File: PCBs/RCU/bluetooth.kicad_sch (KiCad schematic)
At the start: 33 parts

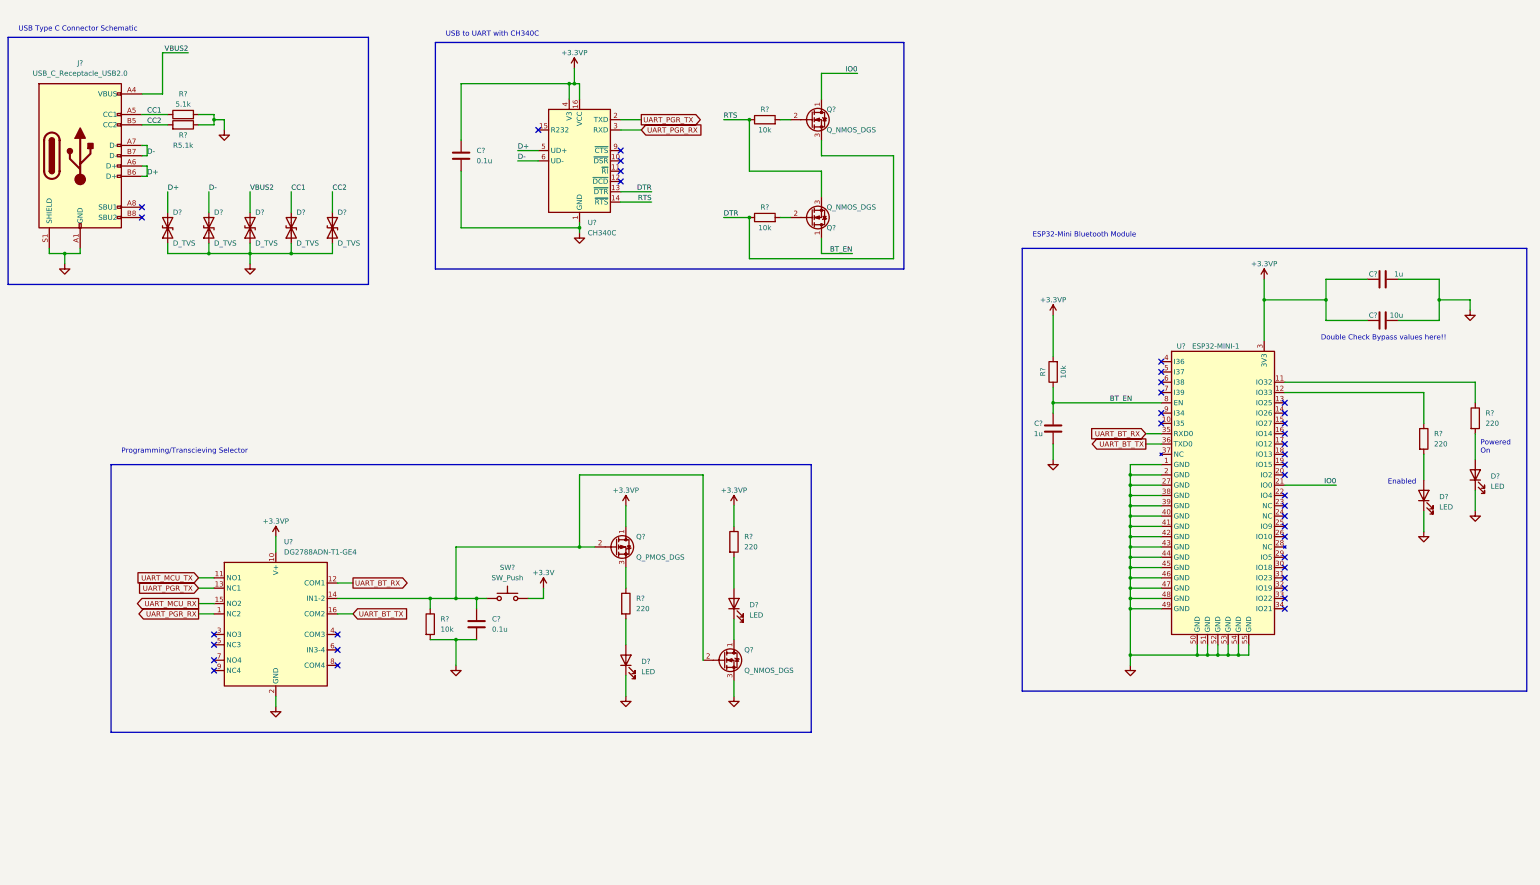
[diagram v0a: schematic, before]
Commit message: Numbered and ordered all of the modules
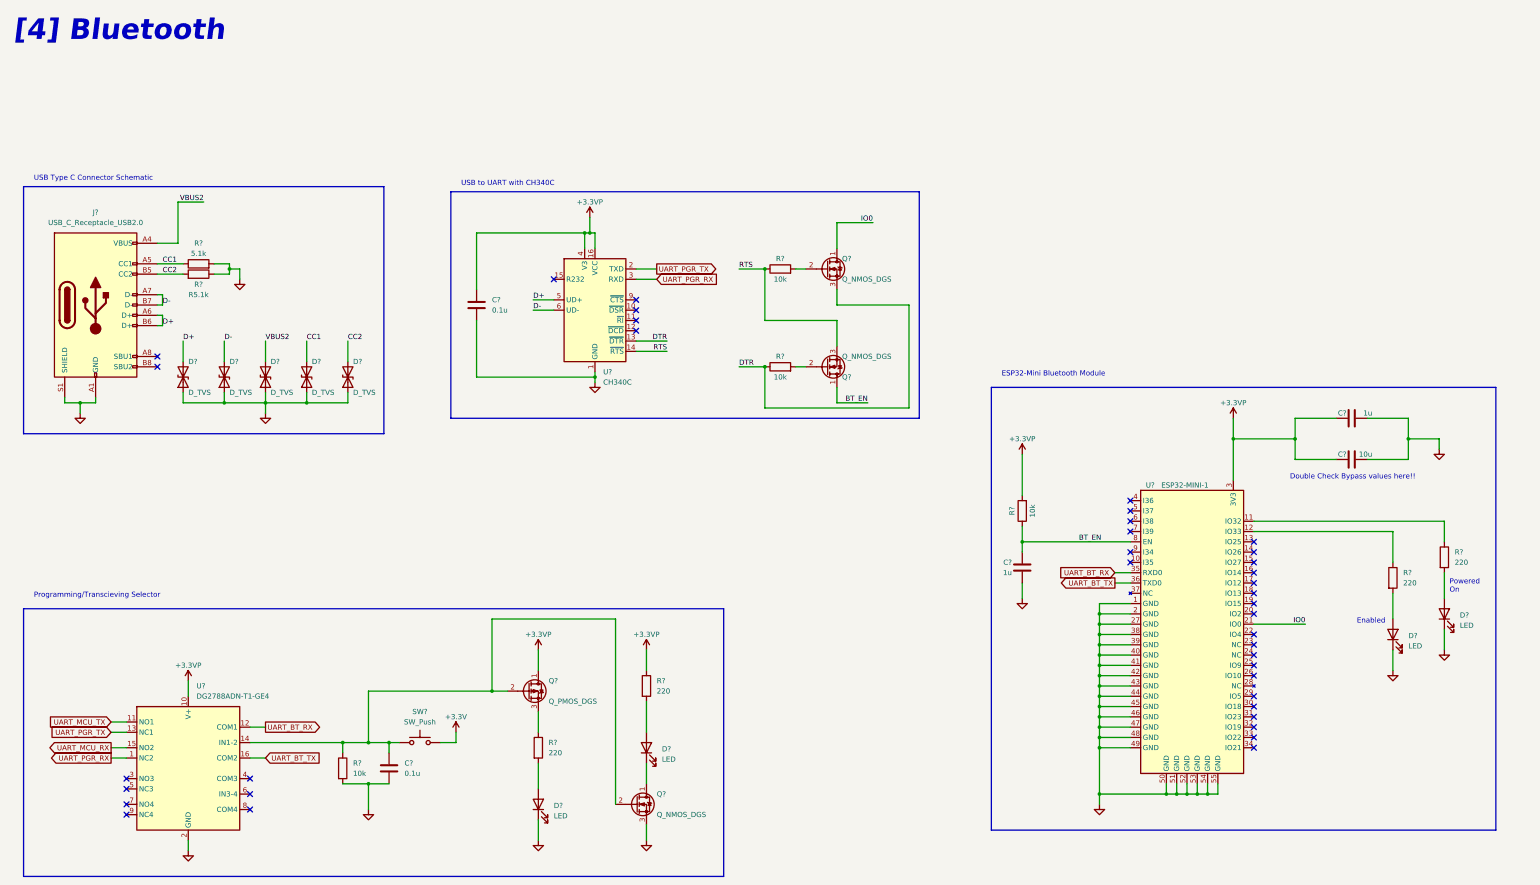
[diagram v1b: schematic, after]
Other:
- note added: "[4] Bluetooth"
- moved on the sheet: C?, D?, J?, Q?, R5.1k, R?, SW?, U?

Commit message: Annotated all components in Bluetooth
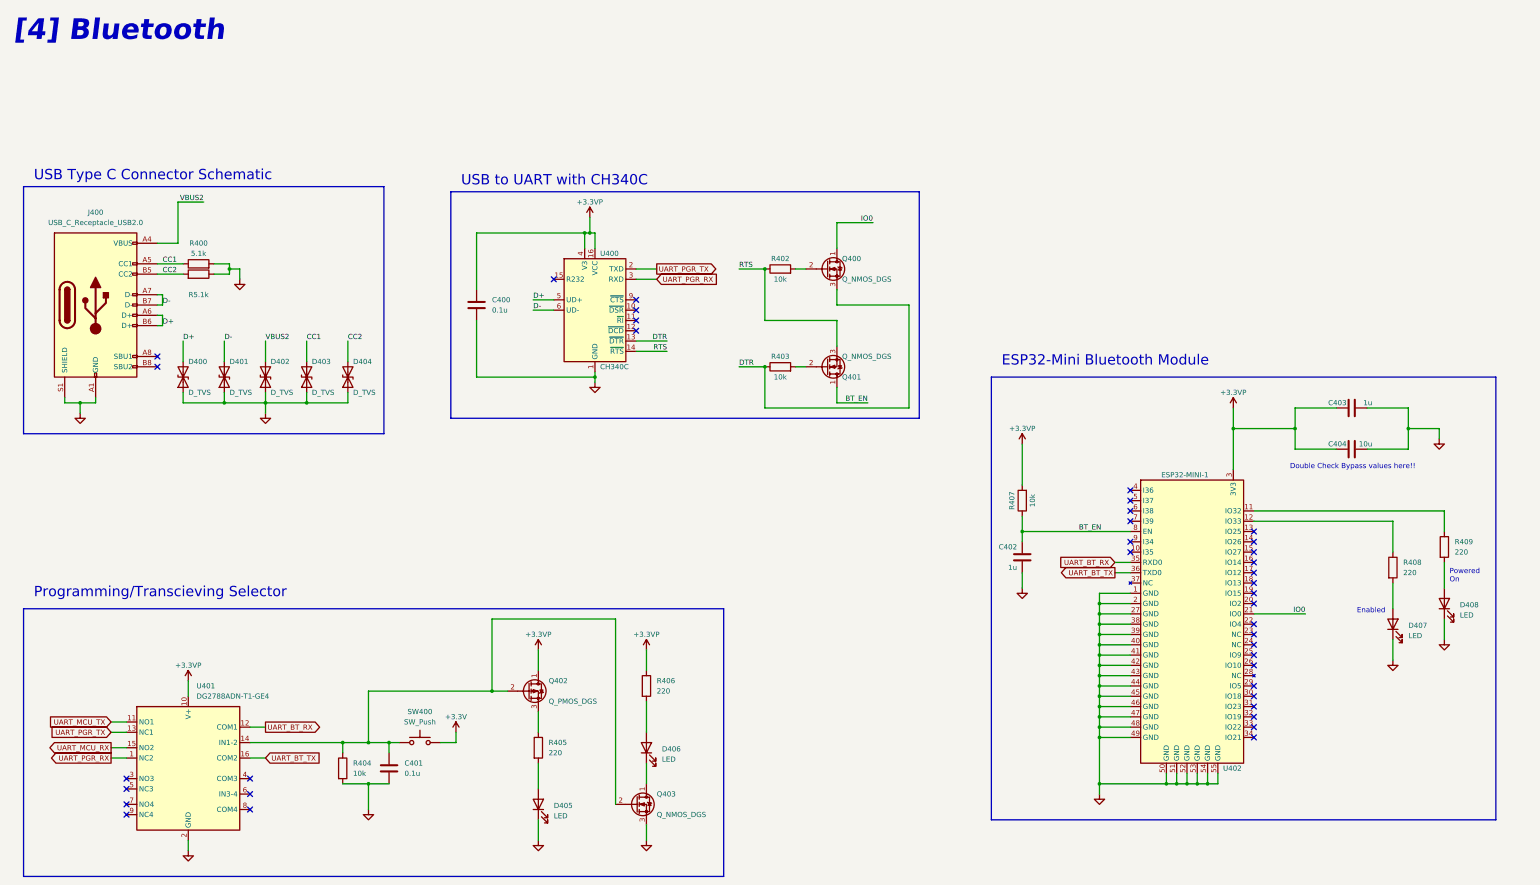
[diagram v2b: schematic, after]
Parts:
- R5.1k: value R? -> (none)
- gave numbers to parts that had none: 32
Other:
- moved on the sheet: C402, C403, C404, D407, D408, R407, R408, R409, U402

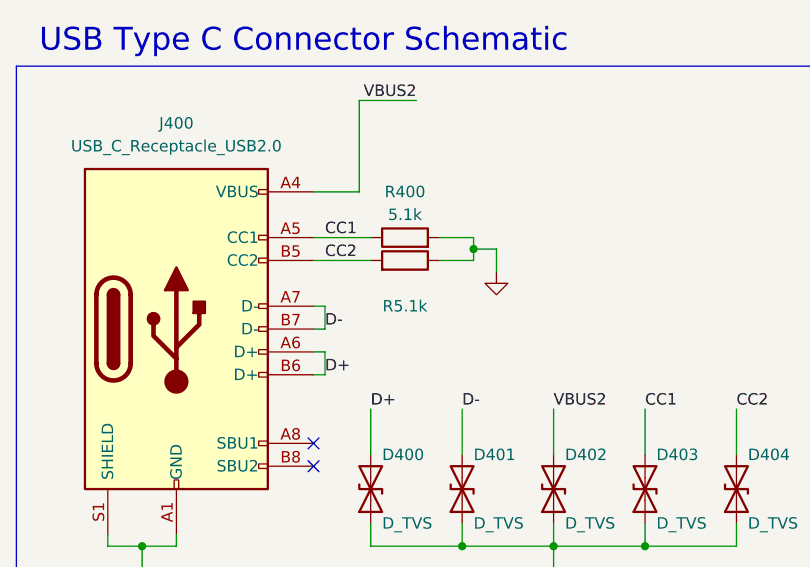
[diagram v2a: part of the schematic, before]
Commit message: The shared SWCLK/BOOT0 pin has an internal pull-down resistor, and in the case where SWCLK is shared and are programming with SWD, just need NRST conncted to the STLink-V2 module
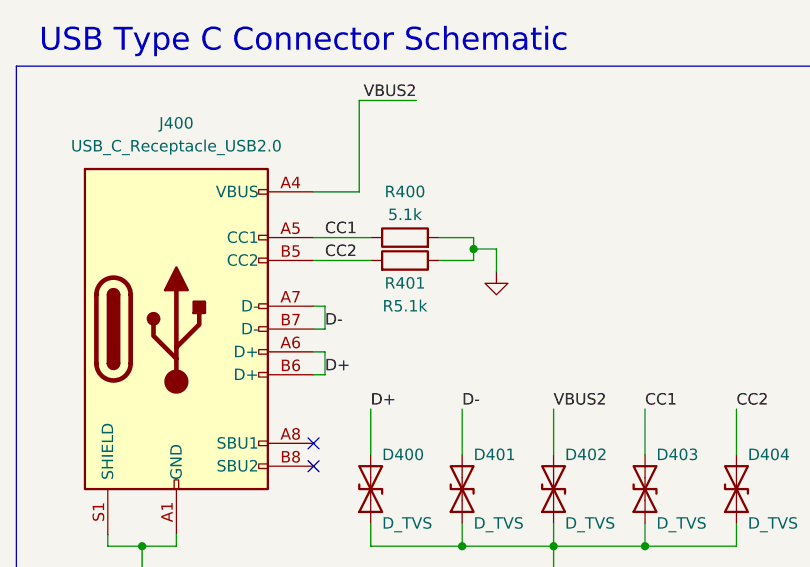
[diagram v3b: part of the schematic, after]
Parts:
- R5.1k: value (none) -> R401
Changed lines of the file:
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@@
     (in_bom yes) (on_board yes)
     (property "Reference" "R5.1k" (id 0) (at 77.47 95.25 90))
-    (property "Value" "" (id 1) (at 77.47 92.71 90))
+    (property "Value" "R401" (id 1) (at 77.47 92.71 90))
     (property "Footprint" "" (id 2) (at 77.47 91.948 90)
       (effects (font (size 1.27 1.27)) hide)

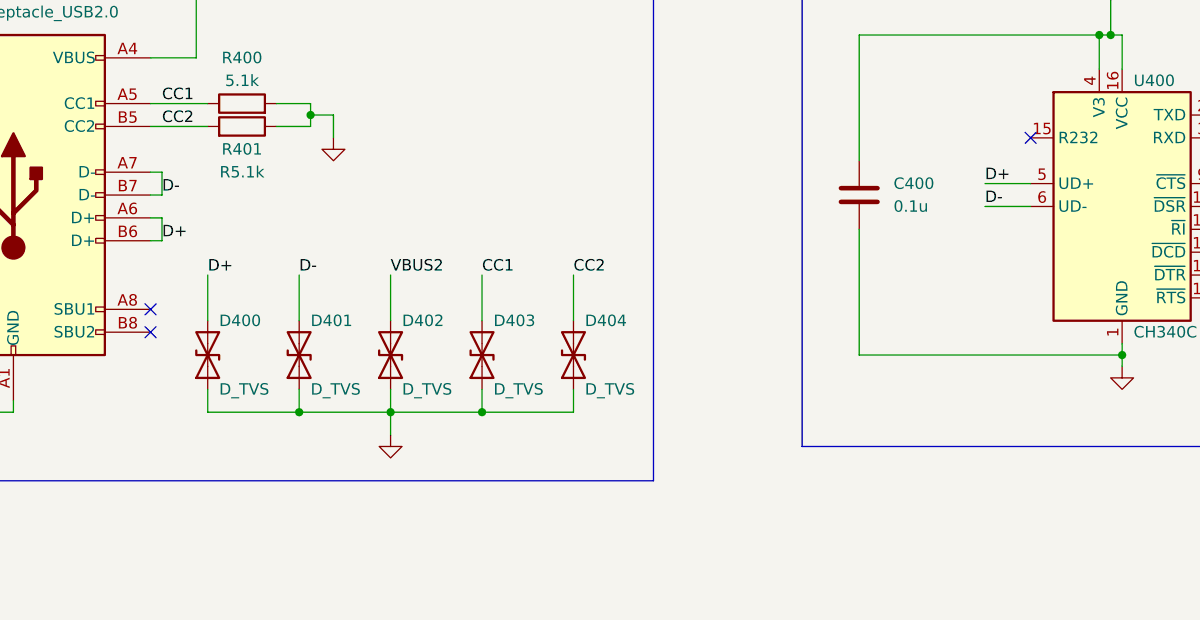
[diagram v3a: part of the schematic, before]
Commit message: Using USBLC-2S6C for ESB protection for usb_c recepticle in bluetooth circuit
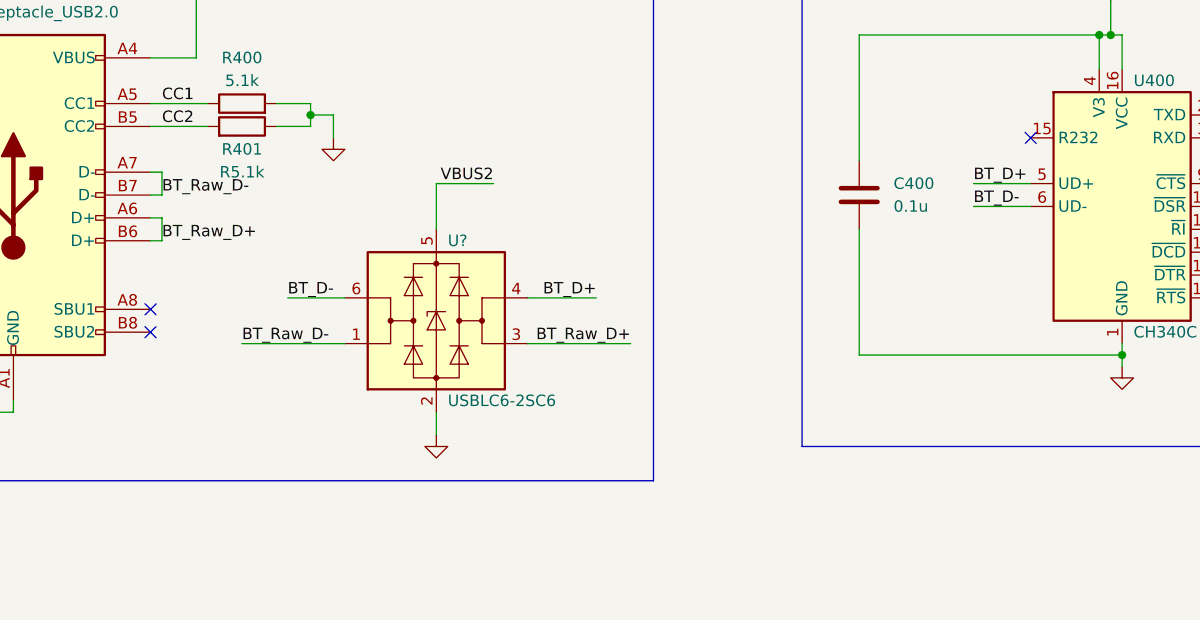
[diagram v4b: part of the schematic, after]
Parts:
- removed D400, D401, D402, D403, D404: D_TVS, symbol Device:D_TVS
- added U?: USBLC6-2SC6, Package_TO_SOT_SMD:SOT-23-6, symbol Power_Protection:USBLC6-2SC6
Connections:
- net GND: now also U?.2 (GND)
- net VBUS2: now also U?.5 (VBUS)
- net D+ renamed BT_Raw_D+
- net BT_Raw_D+: now also U?.3 (I/O2); no longer U400.5 (UD+)
- net D- renamed BT_Raw_D-
- net BT_Raw_D-: now also U?.1 (I/O1); no longer U400.6 (UD-)
- new net BT_D+: U400.5 (UD+), U?.4 (I/O2)
- new net BT_D-: U400.6 (UD-), U?.6 (I/O1)

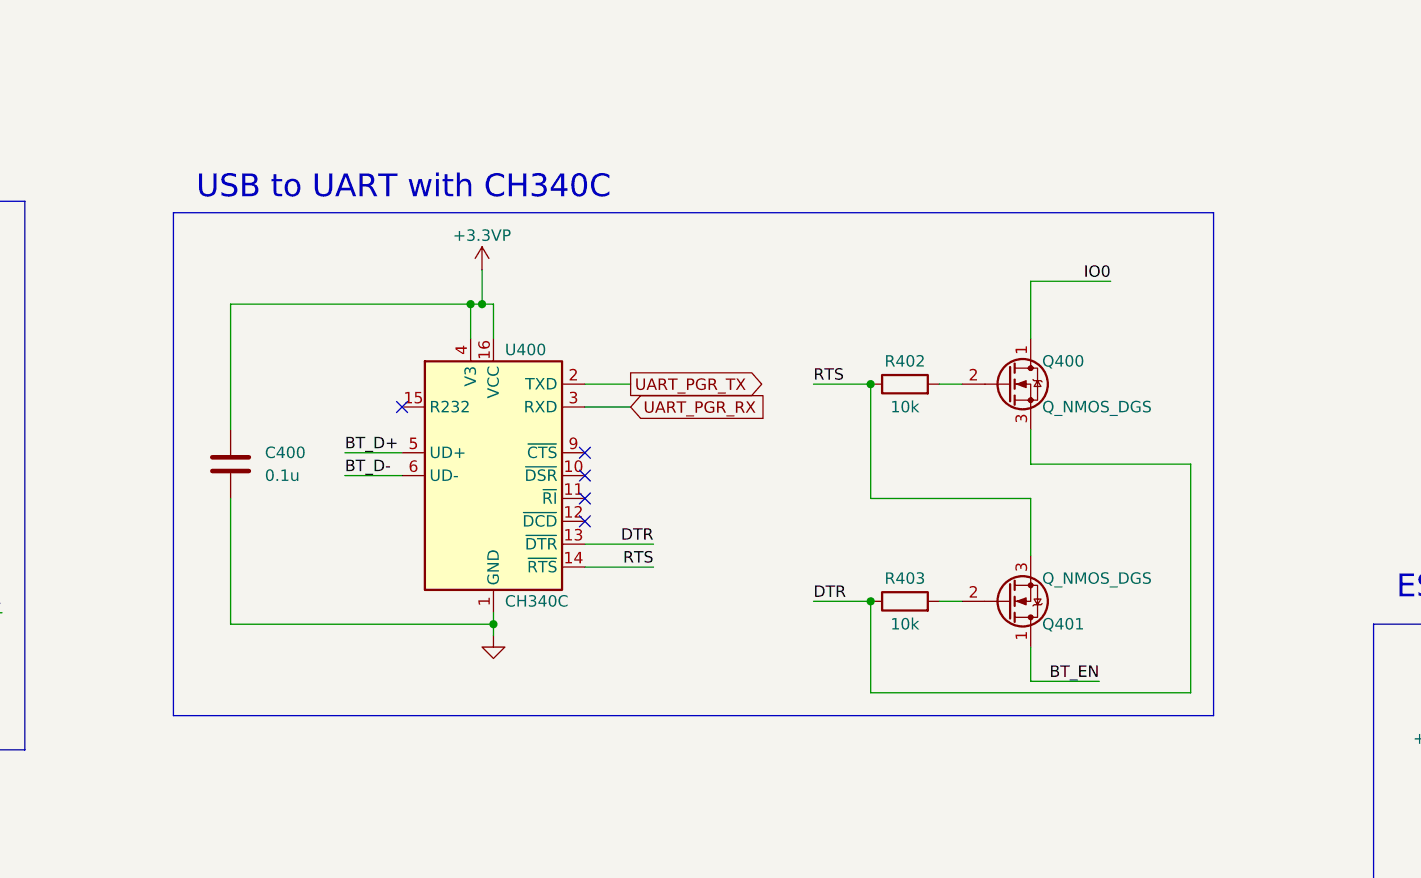
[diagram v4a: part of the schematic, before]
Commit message: Add decoupling capacitors to CH340C IC in Bluetooth module
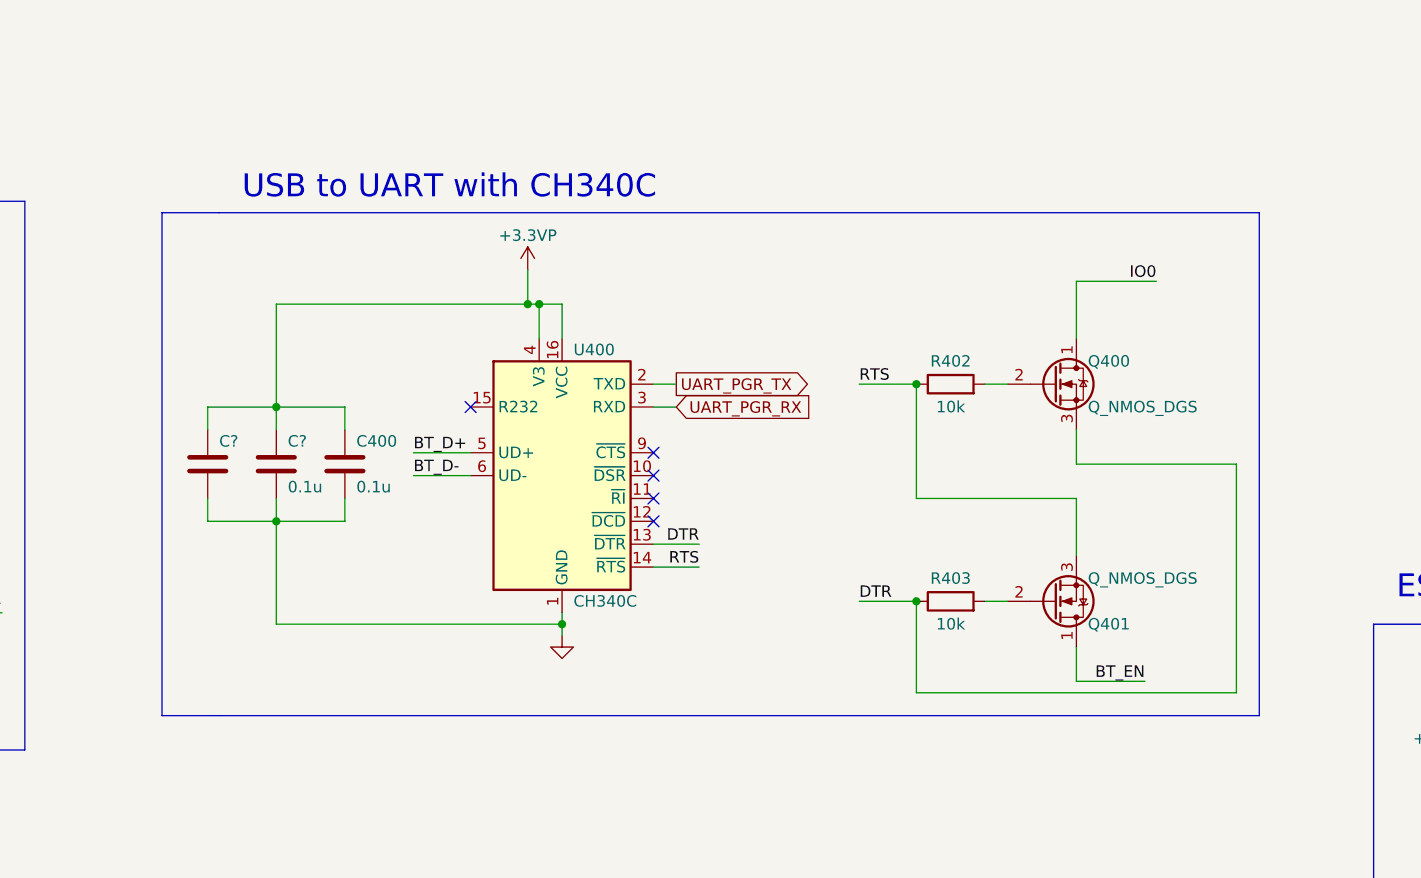
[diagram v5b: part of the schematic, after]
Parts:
- added C?: 0.1u, symbol Device:C
- added C?: (no value), symbol Device:C
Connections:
- net +3.3VP: now also C?.1, C?.1
- net GND: now also C?.2, C?.2
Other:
- moved on the sheet: C400, Q400, Q401, R402, R403, U400
